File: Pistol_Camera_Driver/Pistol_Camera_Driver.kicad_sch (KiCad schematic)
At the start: 102 parts, among them J1 Screw_Terminal_01x02, J10 Bluetooth, J11 Screw_Terminal_01x02, J12 Screw_Terminal_01x02, J13 I2C, J14 Screw_Terminal_01x02, J15 Screw_Terminal_01x02, J2 Objective, J3 Screw_Terminal_01x02, J4 Screw_Terminal_01x02, J5 Screw_Terminal_01x02, J6 Joystick, J7 Screw_Terminal_01x02, J8 Screw_Terminal_01x02, J9 Screw_Terminal_01x02, K1 IM03, M1 Fan, Q1 FFB2222A, U1 LM7805_TO220, U2 LM317_TO-263, U3 Raspberri_Pi_Pico, U4 DRV8834PWP, U5 DRV8834PWP

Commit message: V0.2 Seems 2B ready
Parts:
- removed C23: 2u2, Capacitor_SMD:C_0603_1608Metric_Pad1.08x0.95mm_HandSolder, symbol Device:C
- removed C4, C6: 1, Capacitor_SMD:C_0603_1608Metric_Pad1.08x0.95mm_HandSolder, symbol Device:C
- removed U1: LM7805_TO220, Package_TO_SOT_THT:TO-220-3_Vertical, symbol Regulator_Linear:LM7805_TO220
- removed U2: LM317_TO-263, Package_TO_SOT_SMD:TO-263-2, symbol Regulator_Linear:LM317_TO-263
- removed U3: Raspberri_Pi_Pico, Shield_Emergent:Raspberry Pi Pico, symbol Shield_Emergent:Raspberri_Pi_Pico
- added C4: 470uF, Capacitor_THT:CP_Radial_D6.3mm_P2.50mm, symbol Device:C_Polarized
- added C6: 180uF, Capacitor_THT:CP_Radial_D6.3mm_P2.50mm, symbol Device:C_Polarized
- added D2: CDBA3100-HF, Diode_SMD:D_SMA, symbol Diode:CDBA3100-HF
- added J16, J17: Screw_Terminal_01x02, Connector_PinSocket_2.54mm:PinSocket_1x02_P2.54mm_Vertical, symbol Connector:Screw_Terminal_01x02
- added L5: 22u, Inductor_SMD:L_Sunlord_SWPA4012S, symbol Device:L
- added U1: XL1509-3.3, Package_SO:SOIC-8-1EP_3.9x4.9mm_P1.27mm_EP2.95x4.9mm_Mask2.71x3.4mm_ThermalVias, symbol Vedro:XL1509-3.3
- C13, C15, C16, C17, C19, C20, C22: value 2u2 -> 22u
- C2: value 0.33 -> 0.1
- C3: value 0.1 -> 22u
- L1, L2, L3, L4: value L -> 4u7; footprint Inductor_SMD:L_12x12mm_H8mm -> Inductor_SMD:L_Chilisin_BMRx00040412
- R3: value 240 -> 4k7
- R6: value 390 -> 4k7
- U10: footprint (none) -> Vedro:RP2040Zero
- U4, U5: footprint Shield_Emergent:DRV8834PWP -> Vedro:DRV8834PWP
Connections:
- net +12V is gone; now on net +5V: C14.2, C15.1, C16.1, C18.2, C19.1, C2.1, C21.2, C22.1, C24.2, J3.1 (Pin_1), J4.1 (Pin_1), M1.1 (+), U6.3 (VINA), U6.8 (VINSW), U7.3 (VINA), U7.8 (VINSW), U8.3 (VINA), U8.8 (VINSW), U9.3 (VINA), U9.8 (VINSW)
- net +3.3VP: now also C6.1, D2.1 (K), L5.2, U1.3 (FB); no longer R3.1
- net +3V3: now also J10.3 (Pin_3), J13.4 (Pin_4), R3.1, R6.1, U10.30 (3V3)
- net +5V: now also U10.32 (5V), C4.1, U1.1 (VIN); no longer C3.1, J10.4 (Pin_4), J13.4 (Pin_4)
- net DIR1: now also U10.12 (GP12/TX0/SDA0/MISO1)
- net DIR2: now also U10.26 (GP26/ADC0/SDA1)
- net K1: now also U10.20 (GP20/SDA0)
- net K2: now also U10.21 (GP21/SCL0)
- net K3: now also U10.22 (PG22)
- net K4: now also U10.23 (GP23)
- net MOTORS_nSLEEP: now also U10.18 (GP18/SDA1/SCK0)
- net PWM_IR: now also U10.10 (GP10/SDA1/SCK1)
- net PWM_RED: now also U10.8 (GP8/TX1/SDA0/MISO1), U7.4 (DIM); no longer U8.4 (DIM)
- net PWM_UV: now also U10.9 (GP9/RX1/CS1), U8.4 (DIM); no longer U6.4 (DIM)
- net PWM_WHITE: now also U10.7 (GP7/SCL1/MOSI0), U6.4 (DIM); no longer U7.4 (DIM)
- net RX: now also U10.0 (GP0/TX0/SDA0/MISO0)
- net SCL: now also J13.1 (Pin_1), R3.2, U10.5 (GP5/RX1/SCL0/CS0); no longer J13.2 (Pin_2)
- net SDA: now also J13.2 (Pin_2), R6.2, U10.4 (GP4/TX1/SDA0/MIOS0); no longer J13.1 (Pin_1)
- net STEP1: now also U10.13 (GP13/RX0/SCL0/CS1)
- net STEP2: now also U10.15 (GP15SCL1/MOSI1)
- net SW: now also U10.27 (GP27/ADC1/SCL1)
- net Solenoid_DIR: now also R19.1, U10.3 (GP3/SCL1/MOSI0); no longer R17.1
- net Solenoid_ON: now also R17.1, U10.2 (GP2/SDA1/SCK1); no longer R19.1
- net Strobe Input: now also U10.6 (GP6/SDA1/SCK1)
- net TX: now also U10.1 (GP1/RX0/SCL0/CS0)
- net VarX: now also U10.28 (GP28/ADC2)
- net VarY: now also U10.29 (GP29/ADC3)
- net nEN1: now also U10.11 (GP11/SCL1/MOSI1)
- net nEN2: now also U10.14 (GP14/SDA1/SCK1)
- net nFLT1: now also U10.17 (GP17/RX0/SCL0/CS0)
- net nFLT2: now also U10.19 (GP19/SCL1/MOSI0)
- net at D9.2 (A), J12.1 (Pin_1), L4.2: now also C20.1
- net K5: now reaches U10.24 (GP24)
- net K5: now also J16.1 (Pin_1)
- net K6: now reaches U10.25 (GP25)
- net K6: now also J17.1 (Pin_1)
- net EP: now reaches U10.31 (GND)
- net EP: now also C1.2, C10.2, C12.2, C13.2, C14.1, C15.2, C16.2, C17.2, C18.1, C19.2, C2.2, C20.2, C21.1, C22.2, C24.1, C3.2, C5.1, C8.2, C9.2, J1.2 (Pin_2), J10.4 (Pin_4), J13.3 (Pin_3), J14.2 (Pin_2), J15.2 (Pin_2), J3.2 (Pin_2), J4.2 (Pin_2), J5.2 (Pin_2), J6.1 (Pin_1), J8.2 (Pin_2), M1.2 (-), Q1.1 (E1), Q1.4 (E2), R10.1, R11.1, R12.1, R14.2, R15.2, R16.2, R18.2, R2.1, R20.2, R21.2, R22.2, R23.2, R24.2, R25.2, R26.2, R27.2, R28.2, R29.2, R30.2, R31.2, R32.2, R33.2, R34.2, R35.2, R36.2, R37.2, R38.2, R39.2, R4.1, R5.1, R7.1, R9.1, U10.33 (GND), U4.13 (M0), U4.14 (M1), U4.21 (GND), U4.25 (GND), U5.13 (M0), U5.14 (M1), U5.21 (GND), U5.25 (GND), U6.2 (PGND), U6.6 (AGND), U6.7 (GND), U7.2 (PGND), U7.6 (AGND), U7.7 (GND), U8.2 (PGND), U8.6 (AGND), U8.7 (GND), U9.2 (PGND), U9.6 (AGND), U9.7 (GND), C4.2, C6.2, D2.2 (A), J16.2 (Pin_2), J17.2 (Pin_2), U1.4 (~{EN}), U1.5 (GND), U1.6 (GND), U1.7 (GND), U1.8 (GND), U1.9 (EP)
- net at D5.2 (A), J9.1 (Pin_1), L3.2: now also C3.1; no longer C20.1
- removed net GND: C1.2, C10.2, C12.2, C13.2, C14.1, C15.2, C16.2, C17.2, C18.1, C19.2, C2.2, C20.2, C21.1, C22.2, C24.1, C3.2, C5.1, C8.2, C9.2, J1.2 (Pin_2), J10.3 (Pin_3), J13.3 (Pin_3), J14.2 (Pin_2), J15.2 (Pin_2), J3.2 (Pin_2), J4.2 (Pin_2), J5.2 (Pin_2), J6.1 (Pin_1), J8.2 (Pin_2), M1.2 (-), Q1.1 (E1), Q1.4 (E2), R10.1, R11.1, R12.1, R14.2, R15.2, R16.2, R18.2, R2.1, R20.2, R21.2, R22.2, R23.2, R24.2, R25.2, R26.2, R27.2, R28.2, R29.2, R30.2, R31.2, R32.2, R33.2, R34.2, R35.2, R36.2, R37.2, R38.2, R39.2, R4.1, R5.1, R6.2, R7.1, R9.1, U4.13 (M0), U4.14 (M1), U4.21 (GND), U4.25 (GND), U5.13 (M0), U5.14 (M1), U5.21 (GND), U5.25 (GND), U6.2 (PGND), U6.6 (AGND), U6.7 (GND), U7.2 (PGND), U7.6 (AGND), U7.7 (GND), U8.2 (PGND), U8.6 (AGND), U8.7 (GND), U9.2 (PGND), U9.6 (AGND), U9.7 (GND)
- new net: L5.1, U1.2 (OUT)
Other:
- moved on the sheet: J14, J15, J5, J8

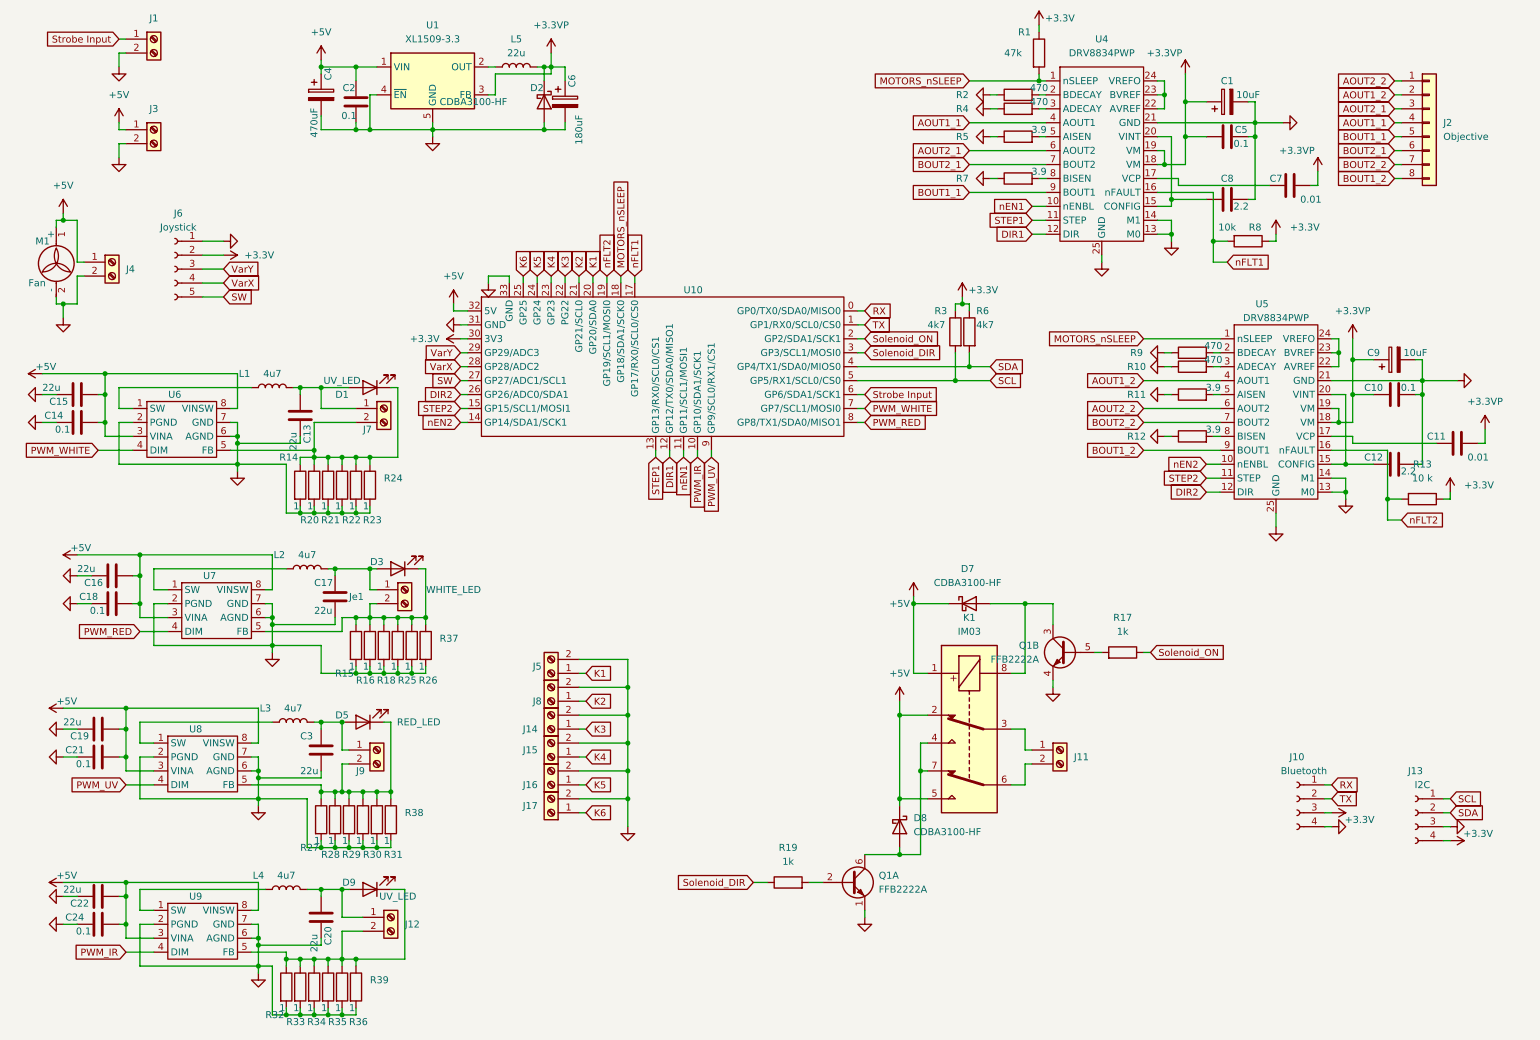
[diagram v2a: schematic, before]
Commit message: v0.4 5 V DC/CD was added, Relay was changed to the H-bridge
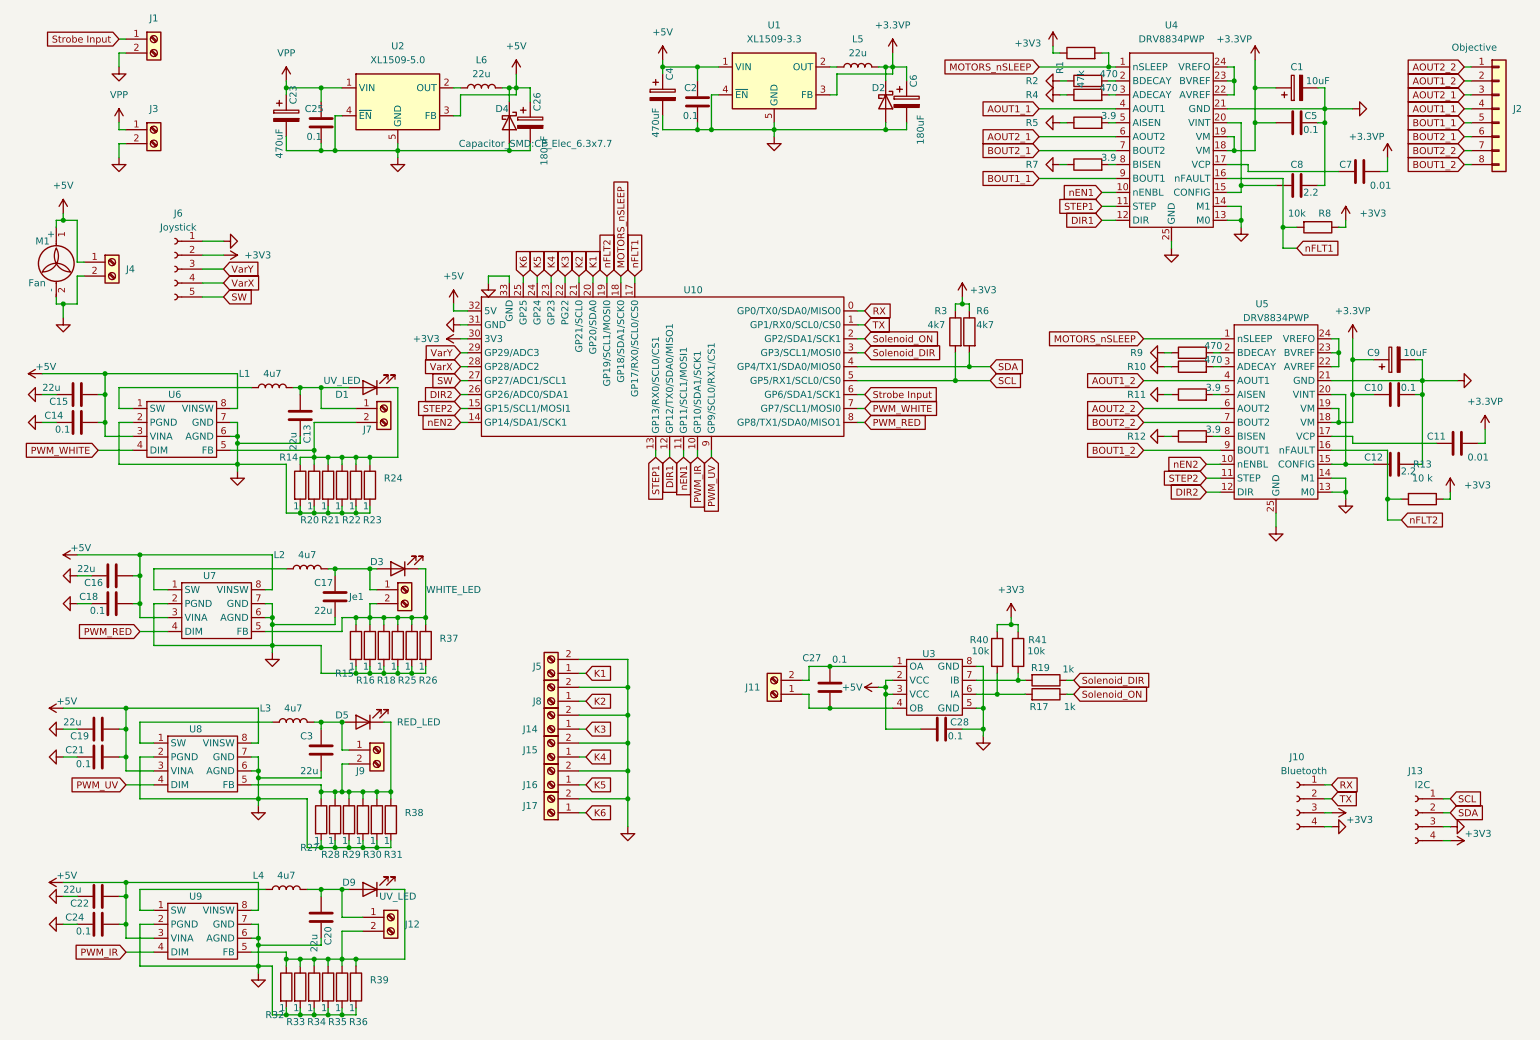
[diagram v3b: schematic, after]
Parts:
- removed D7, D8: CDBA3100-HF, Diode_SMD:D_SMA, symbol Diode:CDBA3100-HF
- removed K1: IM03, Relay_THT:Relay_DPDT_AXICOM_IMSeries_Pitch5.08mm, symbol Relay:IM03
- removed Q1: FFB2222A, Package_TO_SOT_SMD:SOT-363_SC-70-6_Handsoldering, symbol Transistor_BJT:FFB2222A
- added C23: 470uF, Capacitor_SMD:CP_Elec_10x10.5, symbol Device:C_Polarized
- added C25, C27, C28: 0.1, Capacitor_SMD:C_0603_1608Metric_Pad1.08x0.95mm_HandSolder, symbol Device:C
- added C26: 180uF, Capacitor_SMD:CP_Elec_6.3x7.7, symbol Device:C_Polarized
- added D4: CDBA3100-HF, Diode_SMD:D_SMA, symbol Diode:CDBA3100-HF
- added L6: 22u, Inductor_SMD:L_Sunlord_SWPA4012S, symbol Device:L
- added R40, R41: 10k, Resistor_SMD:R_0603_1608Metric_Pad0.98x0.95mm_HandSolder, symbol Device:R
- added U2: XL1509-5.0, Package_SO:SOIC-8-1EP_3.9x4.9mm_P1.27mm_EP2.95x4.9mm_Mask2.71x3.4mm_ThermalVias, symbol Regulator_Switching:XL1509-5.0
- added U3: ~, Package_SO:SOIC-8_3.9x4.9mm_P1.27mm, symbol Vedrofara:L9110S
- C4: footprint Capacitor_THT:CP_Radial_D6.3mm_P2.50mm -> Capacitor_SMD:CP_Elec_10x10.5
- C6: footprint Capacitor_THT:CP_Radial_D6.3mm_P2.50mm -> Capacitor_SMD:CP_Elec_6.3x7.7
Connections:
- net +3V3: now also R40.1, R41.1
- net +5V: now also C26.1, C28.2, D4.1 (K), L6.2, U2.3 (FB), U3.2 (VCC), U3.3 (VCC); no longer J3.1 (Pin_1)
- net EP: now also C23.2, C25.2, C26.2, C28.1, D4.2 (A), U2.4 (~{EN}), U2.5 (GND), U2.6 (GND), U2.7 (GND), U2.8 (GND), U3.5 (GND), U3.8 (GND)
- net at R17.2: now also R40.2, U3.6 (IA)
- net at J11.1 (Pin_1): now also C27.2, U3.4 (OB)
- net at J11.2 (Pin_2): now also C27.1, U3.1 (OA)
- net at R19.2: now also R41.2, U3.7 (IB)
- new net: L6.1, U2.2 (OUT)
- new net VPP: C23.1, C25.1, J3.1 (Pin_1), U2.1 (VIN)
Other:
- moved on the sheet: C1, C2, C4, C5, C6, C7, C8, D2, J11, J2, L5, R1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
